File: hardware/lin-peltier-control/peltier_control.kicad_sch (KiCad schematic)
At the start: 8 parts, among them J4 PELTIER, Q3 2N7002, Q4 SUD50P04-08

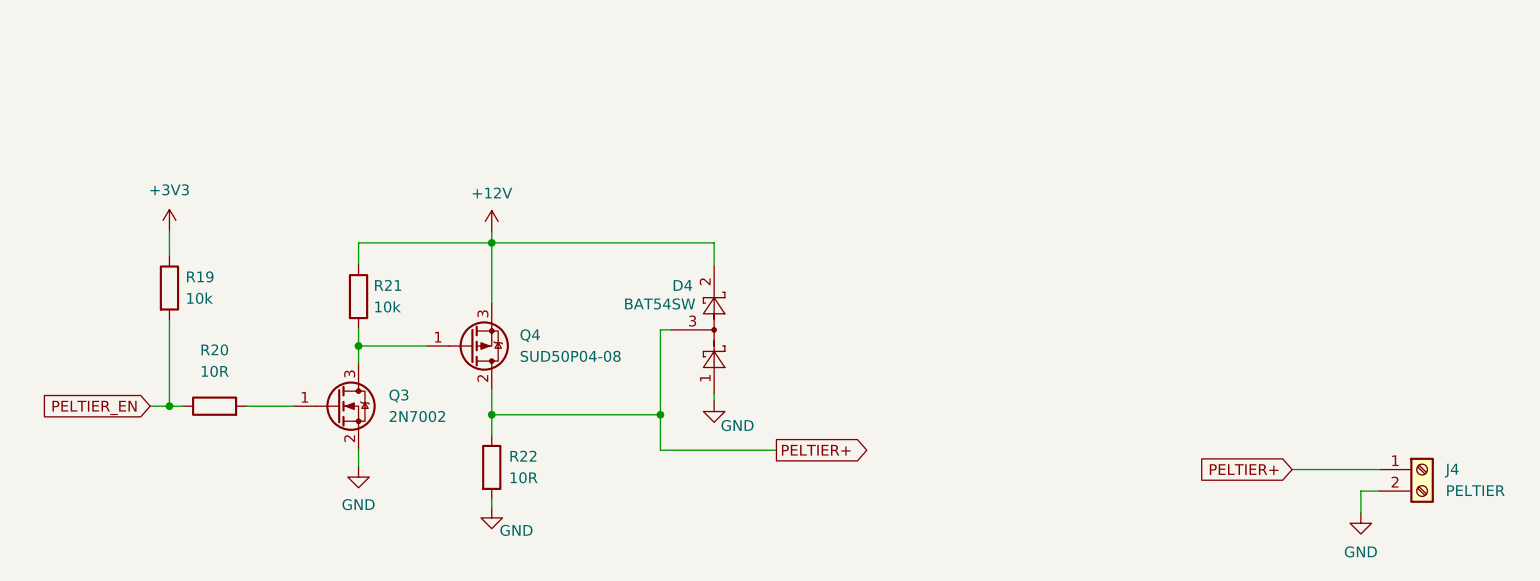
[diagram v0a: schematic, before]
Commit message: Update the peltier controller to include INA219.
- resistor value to be changed in a bit.
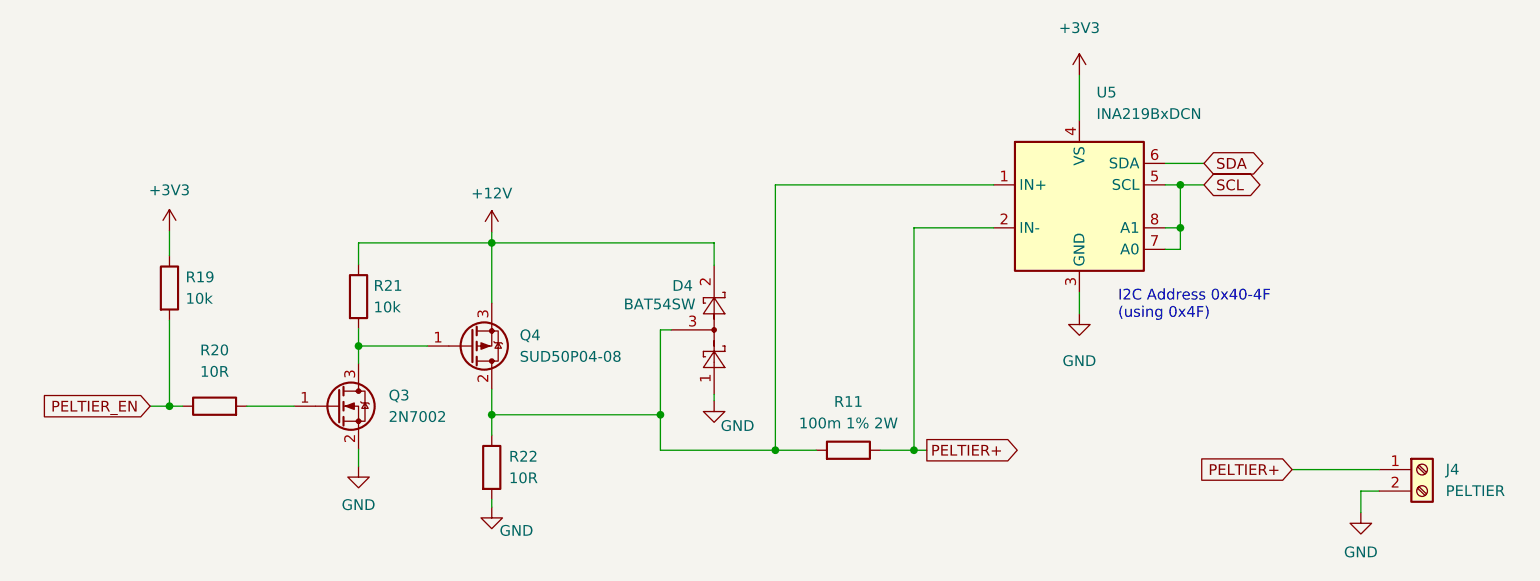
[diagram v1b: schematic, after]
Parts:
- added R11: 100m 1% 2W, Resistor_SMD:R_2512_6332Metric_Pad1.40x3.35mm_HandSolder, symbol Device:R
- added U5: INA219BxDCN, Package_TO_SOT_SMD:SOT-23-8, symbol Beirdo:INA219BxDCN
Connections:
- net +3V3: now also U5.4 (VS)
- net GND: now also U5.3 (GND)
- net PELTIER+: now also R11.1, U5.2 (IN-); no longer D4.3, Q4.2 (D), R22.1
- new net: D4.3, Q4.2 (D), R11.2, R22.1, U5.1 (IN+)
- new net SCL: U5.5 (SCL), U5.7 (A0), U5.8 (A1)
- new net SDA: U5.6 (SDA)
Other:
- note added: "I2C Address 0x40-4F (using 0x4F)"
- title: LINBus Pump Controller -> LINBus Peltier Controller
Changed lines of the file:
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@@
   (paper "A4")
   (title_block
-    (title "LINBus Pump Controller")
-    (date "2023-02-20")
+    (title "LINBus Peltier Controller")
+    (date "2023-03-02")
     (rev "1.0")
     (company "Gavin Hurlbut")
@@
   (junction (at 99.314 102.108) (diameter 0) (color 0 0 0 0)
   )
+  (junction (at 170.942 107.315) (diameter 0) (color 0 0 0 0)
+  )
   (junction (at 157.353 103.124) (diameter 0) (color 0 0 0 0)
   )
+  (junction (at 218.821 75.946) (diameter 0) (color 0 0 0 0)
+  )
+  (junction (at 187.325 107.315) (diameter 0) (color 0 0 0 0)
+  )
+  (junction (at 218.821 81.026) (diameter 0) (color 0 0 0 0)
+  )
   (junction (at 137.414 82.804) (diameter 0) (color 0 0 0 0)
   )
@@
     (stroke (width 0) (type default) (color 0 0 0 0))
   )
+  (wire (pts (xy 206.883 88.646) (xy 206.883 91.186))
+    (stroke (width 0) (type default) (color 0 0 0 0))
+  )
+  (wire (pts (xy 187.325 107.315) (xy 188.849 107.315))
+    (stroke (width 0) (type default) (color 0 0 0 0))
+  )
+  (wire (pts (xy 187.325 81.026) (xy 187.325 107.315))
+    (stroke (width 0) (type default) (color 0 0 0 0))
+  )
+  (wire (pts (xy 217.043 83.566) (xy 218.821 83.566))
+    (stroke (width 0) (type default) (color 0 0 0 0))
+  )
   (wire (pts (xy 240.157 114.681) (xy 240.157 112.141))
     (stroke (width 0) (type default) (color 0 0 0 0))
@@
     (stroke (width 0) (type default) (color 0 0 0 0))
   )
+  (wire (pts (xy 218.821 81.026) (xy 218.821 75.946))
+    (stroke (width 0) (type default) (color 0 0 0 0))
+  )
+  (wire (pts (xy 170.942 75.946) (xy 196.723 75.946))
+    (stroke (width 0) (type default) (color 0 0 0 0))
+  )
   (wire (pts (xy 137.414 103.124) (xy 157.353 103.124))
     (stroke (width 0) (type default) (color 0 0 0 0))
@@
     (stroke (width 0) (type default) (color 0 0 0 0))
   )
+  (wire (pts (xy 218.821 83.566) (xy 218.821 81.026))
+    (stroke (width 0) (type default) (color 0 0 0 0))
+  )
   (wire (pts (xy 163.703 82.804) (xy 163.703 85.471))
     (stroke (width 0) (type default) (color 0 0 0 0))
@@
     (stroke (width 0) (type default) (color 0 0 0 0))
   )
+  (wire (pts (xy 170.942 107.315) (xy 175.768 107.315))
+    (stroke (width 0) (type default) (color 0 0 0 0))
+  )
   (wire (pts (xy 157.353 103.124) (xy 157.353 107.315))
     (stroke (width 0) (type default) (color 0 0 0 0))
   )
+  (wire (pts (xy 217.043 73.406) (xy 221.615 73.406))
+    (stroke (width 0) (type default) (color 0 0 0 0))
+  )
   (wire (pts (xy 137.414 105.537) (xy 137.414 103.124))
     (stroke (width 0) (type default) (color 0 0 0 0))
@@
     (stroke (width 0) (type default) (color 0 0 0 0))
   )
+  (wire (pts (xy 217.043 81.026) (xy 218.821 81.026))
+    (stroke (width 0) (type default) (color 0 0 0 0))
+  )
   (wire (pts (xy 157.353 93.091) (xy 157.353 103.124))
     (stroke (width 0) (type default) (color 0 0 0 0))
   )
+  (wire (pts (xy 196.723 81.026) (xy 187.325 81.026))
+    (stroke (width 0) (type default) (color 0 0 0 0))
+  )
   (wire (pts (xy 99.314 91.948) (xy 99.314 102.108))
     (stroke (width 0) (type default) (color 0 0 0 0))
   )
+  (wire (pts (xy 157.353 107.315) (xy 170.942 107.315))
+    (stroke (width 0) (type default) (color 0 0 0 0))
+  )
   (wire (pts (xy 137.414 82.804) (xy 137.414 89.916))
     (stroke (width 0) (type default) (color 0 0 0 0))
   )
-  (wire (pts (xy 157.353 107.315) (xy 171.069 107.315))
+  (wire (pts (xy 183.388 107.315) (xy 187.325 107.315))
+    (stroke (width 0) (type default) (color 0 0 0 0))
+  )
+  (wire (pts (xy 170.942 75.946) (xy 170.942 107.315))
     (stroke (width 0) (type default) (color 0 0 0 0))
   )
@@
     (stroke (width 0) (type default) (color 0 0 0 0))
   )
+  (wire (pts (xy 206.883 62.992) (xy 206.883 68.326))
+    (stroke (width 0) (type default) (color 0 0 0 0))
+  )
+  (wire (pts (xy 217.043 75.946) (xy 218.821 75.946))
+    (stroke (width 0) (type default) (color 0 0 0 0))
+  )
   (wire (pts (xy 163.703 100.711) (xy 163.703 101.473))
     (stroke (width 0) (type default) (color 0 0 0 0))
   )
+  (wire (pts (xy 218.821 75.946) (xy 221.615 75.946))
+    (stroke (width 0) (type default) (color 0 0 0 0))
+  )
   (wire (pts (xy 99.314 102.108) (xy 97.028 102.108))
     (stroke (width 0) (type default) (color 0 0 0 0))
@@
   (wire (pts (xy 137.414 103.124) (xy 137.414 100.076))
     (stroke (width 0) (type default) (color 0 0 0 0))
+  )
+  (text "I2C Address 0x40-4F\n(using 0x4F)" (at 211.455 91.948 0)
+    (effects (font (size 1.27 1.27)) (justify left bottom))
+  )
+  (global_label "SDA" (shape bidirectional) (at 221.615 73.406 0) (fields_autoplaced)
+    (effects (font (size 1.27 1.27)) (justify left))
+    (property "Intersheet References" "${INTERSHEET_REFS}" (id 0) (at 227.5962 73.3266 0)
+      (effects (font (size 1.27 1.27)) (justify left) hide)
+    )
+  )
+  (global_label "PELTIER+" (shape output) (at 188.849 107.315 0) (fields_autoplaced)
+    (effects (font (size 1.27 1.27)) (justify left))
+    (property "Intersheet References" "${INTERSHEET_REFS}" (id 0) (at 200.1842 107.2356 0)
+      (effects (font (size 1.27 1.27)) (justify left) hide)
+    )
   )
   (global_label "PELTIER+" (shape input) (at 232.029 109.601 180) (fields_autoplaced)
@@
     )
   )
-  (global_label "PELTIER+" (shape output) (at 171.069 107.315 0) (fields_autoplaced)
-    (effects (font (size 1.27 1.27)) (justify left))
-    (property "Intersheet References" "${INTERSHEET_REFS}" (id 0) (at 182.4042 107.2356 0)
-      (effects (font (size 1.27 1.27)) (justify left) hide)
-    )
-  )
   (global_label "PELTIER_EN" (shape input) (at 97.028 102.108 180) (fields_autoplaced)
     (effects (font (size 1.27 1.27)) (justify right))
@@
     )
   )
+  (global_label "SCL" (shape bidirectional) (at 221.615 75.946 0) (fields_autoplaced)
+    (effects (font (size 1.27 1.27)) (justify left))
+    (property "Intersheet References" "${INTERSHEET_REFS}" (id 0) (at 227.5357 75.8666 0)
+      (effects (font (size 1.27 1.27)) (justify left) hide)
+    )
+  )
   (symbol (lib_name "GND_2") (lib_id "power:GND") (at 121.666 109.22 0) (unit 1)
     (in_bom yes) (on_board yes) (fields_autoplaced)
@@
     (pin "1")
   )
+  (symbol (lib_name "+3V3_1") (lib_id "power:+3V3") (at 206.883 62.992 0) (unit 1)
+    (in_bom yes) (on_board yes) (fields_autoplaced)
+    (property "Reference" "#PWR027" (id 0) (at 206.883 66.802 0)
+      (effects (font (size 1.27 1.27)) hide)
+    )
+    (property "Value" "+3V3" (id 1) (at 206.883 57.404 0))
+    (property "Footprint" "" (id 2) (at 206.883 62.992 0)
+      (effects (font (size 1.27 1.27)) hide)
+    )
+    (property "Datasheet" "" (id 3) (at 206.883 62.992 0)
+      (effects (font (size 1.27 1.27)) hide)
+    )
+    (pin "1")
+  )
   (symbol (lib_id "Connector:Screw_Terminal_01x02") (at 247.396 109.601 0) (unit 1)
     (in_bom yes) (on_board yes) (fields_autoplaced)
@@
     (pin "1")
     (pin "2")
+  )
+  (symbol (lib_id "Beirdo:INA219BxDCN") (at 206.883 78.486 0) (unit 1)
+    (in_bom yes) (on_board yes) (fields_autoplaced)
+    (property "Reference" "U5" (id 0) (at 208.9024 65.024 0)
+      (effects (font (size 1.27 1.27)) (justify left))
+    )
+    (property "Value" "INA219BxDCN" (id 1) (at 208.9024 67.564 0)
+      (effects (font (size 1.27 1.27)) (justify left))
+    )
+    (property "Footprint" "Package_TO_SOT_SMD:SOT-23-8" (id 2) (at 223.393 87.376 0)
+      (effects (font (size 1.27 1.27)) hide)
+    )
+    (property "Datasheet" "http://www.ti.com/lit/ds/symlink/ina219.pdf" (id 3) (at 215.773 81.026 0)
+      (effects (font (size 1.27 1.27)) hide)
+    )
+    (pin "1")
+    (pin "2")
+    (pin "3")
+    (pin "4")
+    (pin "5")
+    (pin "6")
+    (pin "7")
+    (pin "8")
   )
   (symbol (lib_id "Device:R") (at 104.648 102.108 90) (unit 1)
@@
     (pin "3")
   )
+  (symbol (lib_name "GND_8") (lib_id "power:GND") (at 206.883 91.186 0) (unit 1)
+    (in_bom yes) (on_board yes) (fields_autoplaced)
+    (property "Reference" "#PWR028" (id 0) (at 206.883 97.536 0)
+      (effects (font (size 1.27 1.27)) hide)
+    )
+    (property "Value" "GND" (id 1) (at 206.883 96.774 0))
+    (property "Footprint" "" (id 2) (at 206.883 91.186 0)
+      (effects (font (size 1.27 1.27)) hide)
+    )
+    (property "Datasheet" "" (id 3) (at 206.883 91.186 0)
+      (effects (font (size 1.27 1.27)) hide)
+    )
+    (pin "1")
+  )
   (symbol (lib_id "Device:R") (at 137.414 109.347 0) (unit 1)
     (in_bom yes) (on_board yes) (fields_autoplaced)
@@
     (pin "1")
   )
+  (symbol (lib_id "Device:R") (at 179.578 107.315 270) (mirror x) (unit 1)
+    (in_bom yes) (on_board yes) (fields_autoplaced)
+    (property "Reference" "R11" (id 0) (at 179.578 101.6 90))
+    (property "Value" "100m 1% 2W" (id 1) (at 179.578 104.14 90))
+    (property "Footprint" "Resistor_SMD:R_2512_6332Metric_Pad1.40x3.35mm_HandSolder" (id 2) (at 179.578 109.093 90)
+      (effects (font (size 1.27 1.27)) hide)
+    )
+    (property "Datasheet" "~" (id 3) (at 179.578 107.315 0)
+      (effects (font (size 1.27 1.27)) hide)
+    )
+    (pin "1")
+    (pin "2")
+  )
 )

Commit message: Convert the peltier controller firmware
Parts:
- R11: value 100m 1% 2W -> 22m 1% 5W
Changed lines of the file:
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@@
     (in_bom yes) (on_board yes) (fields_autoplaced)
     (property "Reference" "R11" (id 0) (at 179.578 101.6 90))
-    (property "Value" "100m 1% 2W" (id 1) (at 179.578 104.14 90))
+    (property "Value" "22m 1% 5W" (id 1) (at 179.578 104.14 90))
     (property "Footprint" "Resistor_SMD:R_2512_6332Metric_Pad1.40x3.35mm_HandSolder" (id 2) (at 179.578 109.093 90)
       (effects (font (size 1.27 1.27)) hide)
